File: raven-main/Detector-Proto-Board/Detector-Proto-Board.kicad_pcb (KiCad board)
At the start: 2 copper layers, 40.2 x 40.4 mm, 43 parts, among them IC1 ADA4817-1ARDZ-R7, J1 Conn_01x04, J2 Conn_01x01, J3 Conn_01x02, U9 TLV3201AIDCKT

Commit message: Replaced LDO with correct one
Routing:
- net /Detector_Out_A: track 70.6 -> 69.6 mm
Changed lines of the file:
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@@
+	)
+	(segment
+		(start 106.706 99.086)
+		(end 105.716 100.076)
+		(width 0.2)
+		(layer "B.Cu")
+		(net "/Detector_Out_A")
+	)
+	(segment
+		(start 123 95)
+		(end 120.142 95)
+		(width 0.2)
+		(layer "B.Cu")
+		(net "/Detector_Out_A")
+	)
+	(segment
+		(start 105.716 100.076)
+		(end 102.87 100.076)
+		(width 0.2)
+		(layer "B.Cu")
+		(net "/Detector_Out_A")
+	)
+	(segment
+		(start 102.87 100.076)
+		(end 101.6 98.806)
+		(width 0.2)
+		(layer "B.Cu")
+		(net "/Detector_Out_A")
+	)
+	(segment
+		(start 120.142 95)
+		(end 116.056 99.086)
+		(width 0.2)
+		(layer "B.Cu")
+		(net "/Detector_Out_A")
+	)
+	(segment
+		(start 96.518 85.596)
+		(end 95.504 85.596)
+		(width 0.2)
+		(layer "B.Cu")
+		(net "/Detector_Out_A")
 	)
 	(segment
 		(start 116.056 99.086)
-		(end 120.142 95)
+		(end 106.706 99.086)
 		(width 0.2)
 		(layer "B.Cu")
@@
 	(segment
 		(start 101.6 90.678)
-		(end 101.6 98.806)
-		(width 0.2)
-		(layer "B.Cu")
-		(net "/Detector_Out_A")
-	)
-	(segment
-		(start 105.716 100.076)
-		(end 106.706 99.086)
+		(end 96.518 85.596)
 		(width 0.2)
 		(layer "B.Cu")
@@
 	(segment
 		(start 101.6 98.806)
-		(end 102.87 100.076)
-		(width 0.2)
-		(layer "B.Cu")
-		(net "/Detector_Out_A")
-	)
-	(segment
-		(start 120.142 95)
-		(end 123 95)
-		(width 0.2)
-		(layer "B.Cu")
-		(net "/Detector_Out_A")
-	)
-	(segment
-		(start 106.706 99.086)
-		(end 116.056 99.086)
-		(width 0.2)
-		(layer "B.Cu")
-		(net "/Detector_Out_A")
-	)
-	(segment
-		(start 98.806 90.678)
 		(end 101.6 90.678)
-		(width 0.2)
-		(layer "B.Cu")
-		(net "/Detector_Out_A")
-	)
-	(segment
-		(start 96.266 88.138)
-		(end 98.806 90.678)
-		(width 0.2)
-		(layer "B.Cu")
-		(net "/Detector_Out_A")
-	)
-	(segment
-		(start 95.504 85.596)
-		(end 96.266 86.358)
-		(width 0.2)
-		(layer "B.Cu")
-		(net "/Detector_Out_A")
-	)
-	(segment
-		(start 96.266 86.358)
-		(end 96.266 88.138)
-		(width 0.2)
-		(layer "B.Cu")
-		(net "/Detector_Out_A")
-	)
-	(segment
-		(start 102.87 100.076)
-		(end 105.716 100.076)
 		(width 0.2)
 		(layer "B.Cu")
@@
 	)
 	(via
-		(at 122.428 93.472)
+		(at 125.5268 90.7288)
 		(size 0.6)
 		(drill 0.3)
@@
 	)
 	(via
-		(at 110.818 87.81)
+		(at 111.3536 89.662)
 		(size 0.6)
 		(drill 0.3)
@@
 	)
 	(segment
-		(start 104.288 81.095)
-		(end 106.865 81.095)
-		(width 0.2)
-		(layer "F.Cu")
-		(net "/OUT")
-	)
-	(segment
-		(start 106.865 81.095)
-		(end 106.934 81.026)
-		(width 0.2)
-		(layer "F.Cu")
-		(net "/OUT")
-	)
-	(segment
 		(start 96.266 80.772)
 		(end 96.266 81.024)
@@
 	)
 	(via
-		(at 106.934 81.026)
+		(at 104.288 81.095)
 		(size 0.6)
 		(drill 0.3)
@@
 	)
 	(segment
-		(start 109.543 83.635)
-		(end 109.712 83.635)
-		(width 0.2)
-		(layer "B.Cu")
-		(net "/OUT")
-	)
-	(segment
 		(start 104.14 94.996)
 		(end 104.14 88.9)
@@
 	)
 	(segment
-		(start 106.934 81.026)
-		(end 109.543 83.635)
-		(width 0.2)
-		(layer "B.Cu")
+		(start 106.828 83.635)
+		(end 104.288 81.095)
+		(width 0.2)
+		(layer "B.Cu")
+		(net "/OUT")
+	)
+	(segment
+		(start 109.712 83.635)
+		(end 106.828 83.635)
+		(width 0.2)
+		(layer "B.Cu")

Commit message: Optional rerouting for lower impedence
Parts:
- moved C39 2.69 mm to (102.1, 75.4), turned to 90 degrees
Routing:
- net /Detector_Out_A: track 69.6 -> 63.6 mm
- net Net-(D1-A2): track 32.1 -> 27.8 mm
- net +5V: track 45.7 -> 43.7 mm, vias 3 -> 2
- net /Vped: track 41.0 -> 42.7 mm
- net Net-(D4-K): track 24.3 -> 25.6 mm, vias 1 -> 2
- net Net-(D4-A): track 35.9 -> 36.8 mm
- net /V_thresh_A: track 57.1 -> 57.9 mm, vias 3 -> 2
- net GND: vias 14 -> 19

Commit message: power board done
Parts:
- removed J1: Conn_01x04, Connector_PinHeader_2.54mm:PinHeader_1x04_P2.54mm_Vertical
- removed J2: Conn_01x01, Connector_PinHeader_2.54mm:PinHeader_1x01_P2.54mm_Vertical
- added J4: Conn_01x03_Pin, Connector_Molex:Molex_Nano-Fit_105313-xx03_1x03_P2.50mm_Horizontal, F.Cu at (121.8, 73.1)
- J3: value Conn_01x02 -> Conn_01x02_Pin; footprint Connector_PinHeader_2.54mm:PinHeader_1x02_P2.54mm_Vertical -> Connector_Molex:Molex_Nano-Fit_105313-xx02_1x02_P2.50mm_Horizontal
- moved G*** 8.01 mm to (121.1, 64.8)
- moved J3 7.22 mm to (102.5, 77.2), turned to 180 degrees
- moved R32 6.55 mm to (119.1, 71.6)
- moved R29 4.79 mm to (115.4, 69.9)
- moved C39 4.02 mm to (102.6, 71.4)
- moved C40 2.91 mm to (123.4, 81.4)
- moved D5 2.13 mm to (106.0, 69.1)
- moved D4 1.62 mm to (105.8, 75.7)
- moved R34 0.73 mm to (121.4, 81.5)
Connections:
- net /V_thresh_A renamed /V_thresh
- J3 pad 1: Net-(D4-K) -> /Detector_Out
- J3 pad 2: Net-(D4-A) -> GND
- R2 pad 2: /Detector_Out_A -> /Detector_Out
- R3 pad 1: /Detector_Out_A -> /Detector_Out
- TP4 pad 1: /Detector_Out_A -> /Detector_Out
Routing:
- net /Detector_Out_A: track 63.6 -> 0.00 mm, vias 3 -> 0
- net /Detector_Out: track 0.00 -> 63.6 mm, vias 0 -> 3
- net /V_thresh: track 57.9 -> 55.3 mm

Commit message: updated detector - need to order
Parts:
- removed C35, C42: 0.5pF, Capacitor_SMD:C_0402_1005Metric
- removed C36: 10uF, Capacitor_SMD:C_0402_1005Metric
- removed C37, C38, C39: 100nF, Capacitor_SMD:C_0402_1005Metric
- removed C40: 1uF, Capacitor_SMD:C_0402_1005Metric
- removed the D1 at (119.4, 88.9)
- removed the G*** at (105.0, 85.0)
- removed the G*** at (119.0, 84.0)
- removed R27, R37: 1G, Resistor_SMD:R_0402_1005Metric
- removed R29: R_Variable, 3224X:SOT_502E
- removed R30: 10K, Resistor_SMD:R_0402_1005Metric
- removed R31: 390K, Resistor_SMD:R_0402_1005Metric
- removed R32: 33, Resistor_SMD:R_0402_1005Metric
- removed R33, R34: 10k, Resistor_SMD:R_0402_1005Metric
- removed R35: 1.6k, Resistor_SMD:R_0402_1005Metric
- removed R38: 0, Resistor_SMD:R_0402_1005Metric
- removed the TP1 at (104.1, 97.5)
- removed TP4: Detector_Out, TestPoint:TestPoint_Pad_D2.5mm
- added C2: 1uF, Capacitor_SMD:C_0603_1608Metric, F.Cu at (109.2, 73.3)
- added C3: 1pF, Capacitor_SMD:C_0402_1005Metric, F.Cu at (111.8, 74.1)
- added C4: 100nF, Capacitor_SMD:C_0402_1005Metric, F.Cu at (112.0, 82.4)
- added C5: 10uF, Capacitor_SMD:C_0805_2012Metric, F.Cu at (114.1, 80.0)
- added C6: 330pF, Capacitor_SMD:C_0402_1005Metric, F.Cu at (113.5, 85.2)
- added C7: 100nF, Capacitor_SMD:C_0402_1005Metric, F.Cu at (116.5, 86.1)
- added G***: LOGO, LOGO, B.Cu at (117.5, 84.2)
- added J2: Conn_01x01, Connector_PinHeader_2.54mm:PinHeader_1x01_P2.54mm_Vertical, F.Cu at (113.9, 88.0)
- added R10: 0Ω, Resistor_SMD:R_0402_1005Metric, F.Cu at (112.1, 85.7)
- added R11: 1.6kΩ, Resistor_SMD:R_0402_1005Metric, F.Cu at (112.1, 84.7)
- added R12: 390kΩ, Resistor_SMD:R_0402_1005Metric, F.Cu at (113.5, 82.7)
- added R13: 1kΩ, Resistor_SMD:R_0402_1005Metric, F.Cu at (118.1, 84.0)
- added R14: 2kΩ, Resistor_SMD:R_0402_1005Metric, F.Cu at (119.6, 84.5)
- added R4: 10kΩ, Resistor_SMD:R_0402_1005Metric, F.Cu at (109.5, 72.1)
- added R5: 1GΩ, Resistor_SMD:R_0402_1005Metric, F.Cu at (111.8, 73.1)
- added R6: 1GΩ, Resistor_SMD:R_0402_1005Metric, F.Cu at (111.8, 72.1)
- added R7: 33Ω, Resistor_SMD:R_0402_1005Metric, F.Cu at (107.1, 81.4)
- added RV1: 3214W-1-102E, Potentiometer_SMD:Potentiometer_Bourns_3214W_Vertical, F.Cu at (108.4, 84.5)
- added TP2: 25V, TestPoint:TestPoint_Pad_D2.0mm, F.Cu at (124.5, 92.5)
- added TP6: Detector_Out, TestPoint:TestPoint_Pad_D2.0mm, F.Cu at (121.2, 92.5)
- C1: value 330p -> 100nF 50V
- R1: value 0 -> 10kΩ
- R2: value 1k -> 10kΩ
- R3: value 2k -> 0Ω
- R9: renamed from R28; value 100k -> 100kΩ
- TP1: renamed from TP3; footprint TestPoint:TestPoint_Pad_D2.5mm -> TestPoint:TestPoint_Pad_D2.0mm
- TP3: renamed from TP2; footprint TestPoint:TestPoint_Pad_D2.5mm -> TestPoint:TestPoint_Pad_D2.0mm
- TP5: value GND -> OUT; footprint TestPoint:TestPoint_Pad_D2.5mm -> TestPoint:TestPoint_Pad_D2.0mm
- moved C1 30.7 mm to (121.1, 69.6), turned to 0 degrees
- moved R2 23.1 mm to (111.0, 69.0), turned to -90 degrees
- moved J3 20.1 mm to (121.8, 83.2), turned to 0 degrees
- moved R3 19.4 mm to (110.0, 70.7), turned to -90 degrees
- moved U1 17.8 mm to (115.3, 83.9), turned to -90 degrees
- moved D1 13.6 mm to (119.0, 72.8), turned to 180 degrees
- moved D2 13.1 mm to (119.0, 68.0), turned to 180 degrees
- moved R9 12.5 mm to (111.6, 87.2), turned to -90 degrees
- moved H4 10.8 mm to (107.0, 91.0)
- moved D3 9.60 mm to (118.4, 80.0)
- moved H1 9.06 mm to (107.0, 68.0)
- moved TP5 7.95 mm to (114.8, 92.5), turned to 90 degrees
- moved R1 6.50 mm to (121.1, 70.6), turned to 180 degrees
- moved H2 6.32 mm to (129.0, 91.0)
- moved IC1 5.94 mm to (110.6, 78.2), turned to -90 degrees
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- renumbered D4 to D1, D5 to D2, D2 to D3, H101 to H1, H102 to H2, H103 to H3, H104 to H4, J4 to J1, U9 to U1
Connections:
- C1 pad 1: Net-(U9-IN-) -> Net-(D1-K)
- D1 pad 1: Net-(D4-K) -> Net-(D1-K)
- D2 pad 1: Net-(D4-K) -> Net-(D1-K)
- J1 pad 1: Net-(D1-A2) -> +25V
- R1 pad 1: Net-(R1-Pad1) -> +25V
- R1 pad 2: /V_thresh -> Net-(D1-K)
- R2 pad 1: Net-(U9-OUT) -> +5V
- R2 pad 2: /Detector_Out -> Net-(R2-Pad2)
- R3 pad 1: /Detector_Out -> Net-(R2-Pad2)
- R3 pad 2: GND -> /Vped
- R9 pad 1: Net-(R1-Pad1) -> Net-(R10-Pad1)
- TP5 pad 1: GND -> /OUT
- U1 pad 1: Net-(U9-OUT) -> /Detector_Out_5V
- U1 pad 4: Net-(U9-IN-) -> Net-(U1-IN-)
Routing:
- net /Detector_Out: track 63.6 -> 12.4 mm, vias 3 -> 2
- net /V_thresh: track 55.3 -> 17.3 mm, vias 2 -> 0
- net Net-(D1-K): track 0.00 -> 37.0 mm, vias 0 -> 2
- net Net-(D1-A2): track 27.8 -> 0.00 mm, vias 2 -> 0
- net Net-(D4-K): track 25.6 -> 0.00 mm, vias 2 -> 0
- net Net-(D1-A): track 36.8 -> 12.4 mm
- net +5V: track 43.7 -> 62.4 mm, vias 2 -> 0
- net /Vped: track 42.7 -> 26.2 mm, vias 5 -> 1
- net +25V: track 13.2 -> 3.39 mm, vias 2 -> 0
- net /OUT: track 36.3 -> 27.8 mm, vias 4 -> 0
- net /Detector_Out_5V: track 0.00 -> 5.46 mm
- net Net-(R29-Pad2): track 4.07 -> 0.00 mm
- net Net-(R1-Pad1): track 3.33 -> 0.00 mm
- net Net-(R10-Pad1): track 0.00 -> 3.26 mm
- net Net-(U9-OUT): track 3.07 -> 0.00 mm
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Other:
- board size 40.2 x 40.4 mm -> 28.5 x 29.5 mm
- board text added: "25V"
- board text added: "5V"
- board text added: "Det"
- board text added: "GND"
- board text added: "HARRIER-Rayquaza v1.0"
- board text added: "HARRIER-Rayquaza v1.0 2026"
- board text added: "Out"
- board text added: "Vin"
- board text added: "Vped"
- board text added: "Vthresh"
- board text removed: "HARRIER v1.0 Detector"

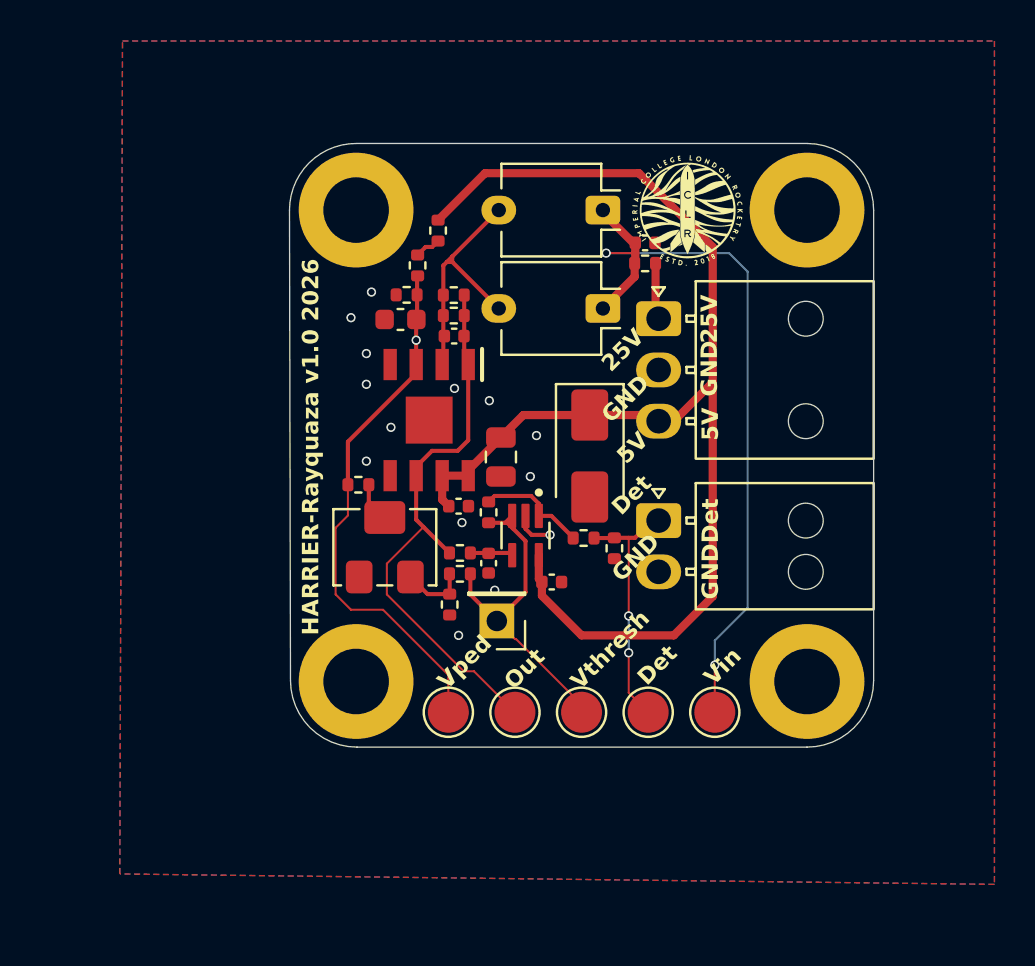
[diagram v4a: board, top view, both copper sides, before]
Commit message: new docs/3d files
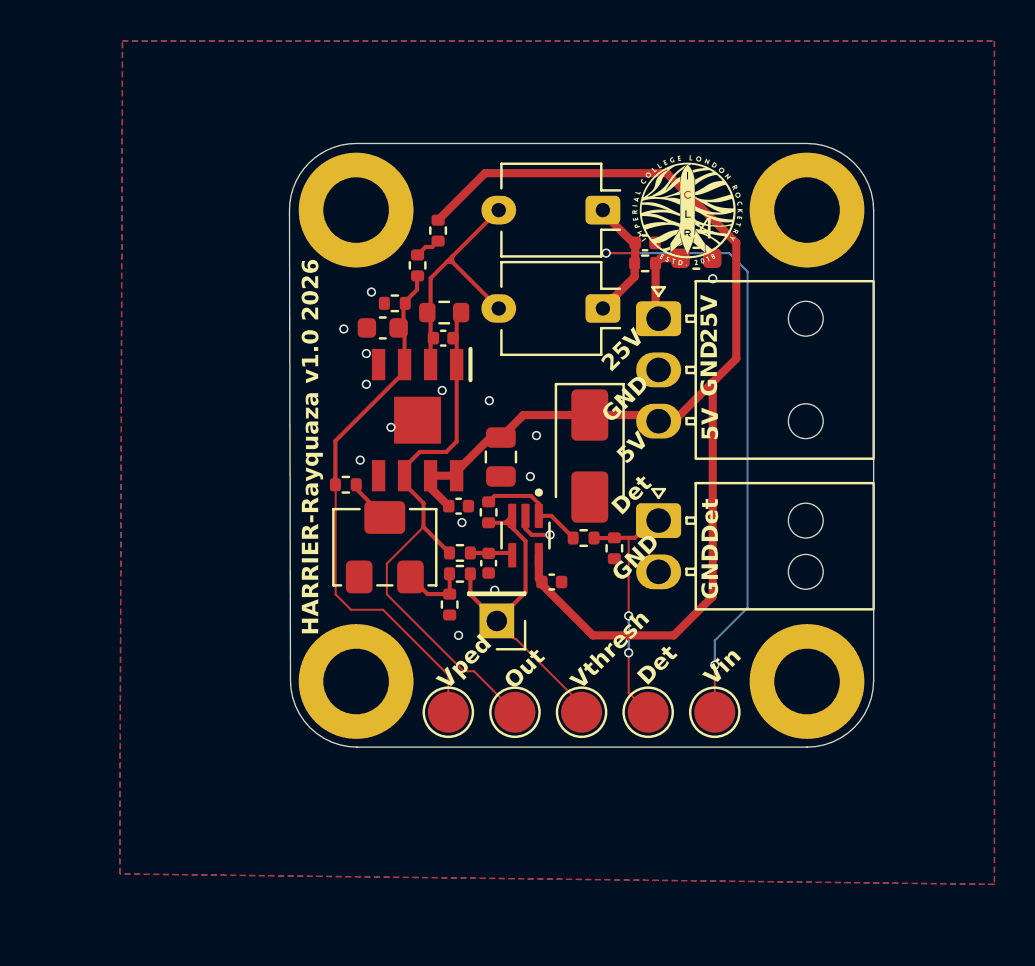
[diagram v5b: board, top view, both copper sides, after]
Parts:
- removed the R5 at (111.8, 73.1)
- added C4: 1uF, Capacitor_SMD:C_0603_1608Metric, F.Cu at (123.6, 70.3)
- D3: value SMAJ5.0A -> SMAJ6.0A
- R5: renamed from R6; value 1GΩ -> 470MΩ; footprint Resistor_SMD:R_0402_1005Metric -> Resistor_SMD:R_0603_1608Metric
- moved R5 0.97 mm to (111.3, 73.0)
- moved C2 0.96 mm to (108.3, 73.8)
- moved R4 0.71 mm to (108.9, 72.5)
- moved R6 0.61 mm to (106.5, 81.4)
- moved IC1 0.57 mm to (110.0, 78.2)
- moved C3 0.54 mm to (111.2, 74.2)
- renumbered C4 to C5, C5 to C6, C6 to C7, C7 to C8, R12 to R10, R13 to R11, R14 to R12, R7 to R6, R9 to R7, R10 to R8, R11 to R9, TP5 to TP4, TP6 to TP5
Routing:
- net +5V: track 62.4 -> 64.4 mm
- net +25V: track 3.39 -> 4.70 mm
- net /OUT: track 27.8 -> 27.2 mm
- net /Vped: track 26.2 -> 26.6 mm, vias 1 -> 0
- net GND: vias 14 -> 15
